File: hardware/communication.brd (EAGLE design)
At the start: 33.5 x 34.6 mm, 34 parts, among them J1 MICRO_USB_B_HIROSE_ZX62-B-5PA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, SW1 TVAF06-A020B-R, U2 NJM12888F, X1 FA-238

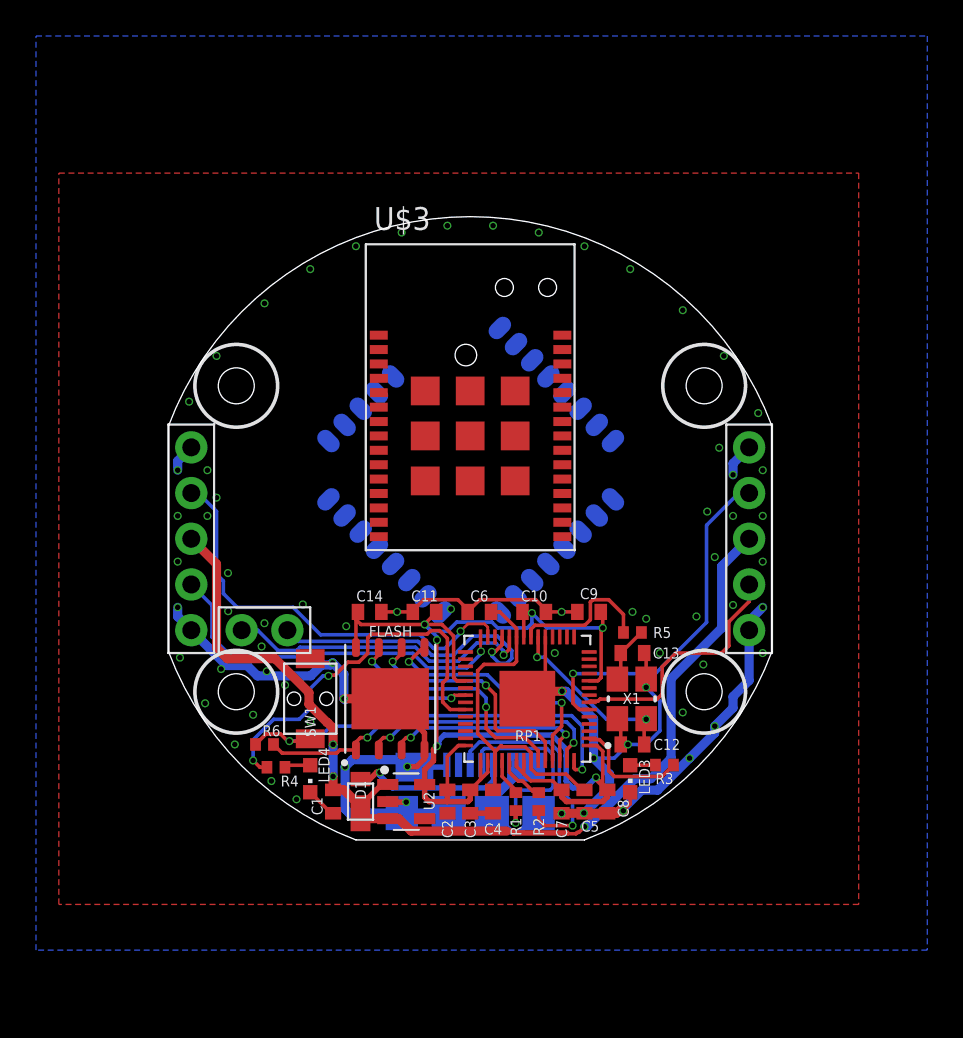
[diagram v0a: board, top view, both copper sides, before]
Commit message: communicationの回路図と基盤の途中経過です。Lo-Raの部分が終わって、残りはTweLiteをやれば完成のはずです。初めて基盤の設計をしているので不備が必ずあると思います。確認お願いします。
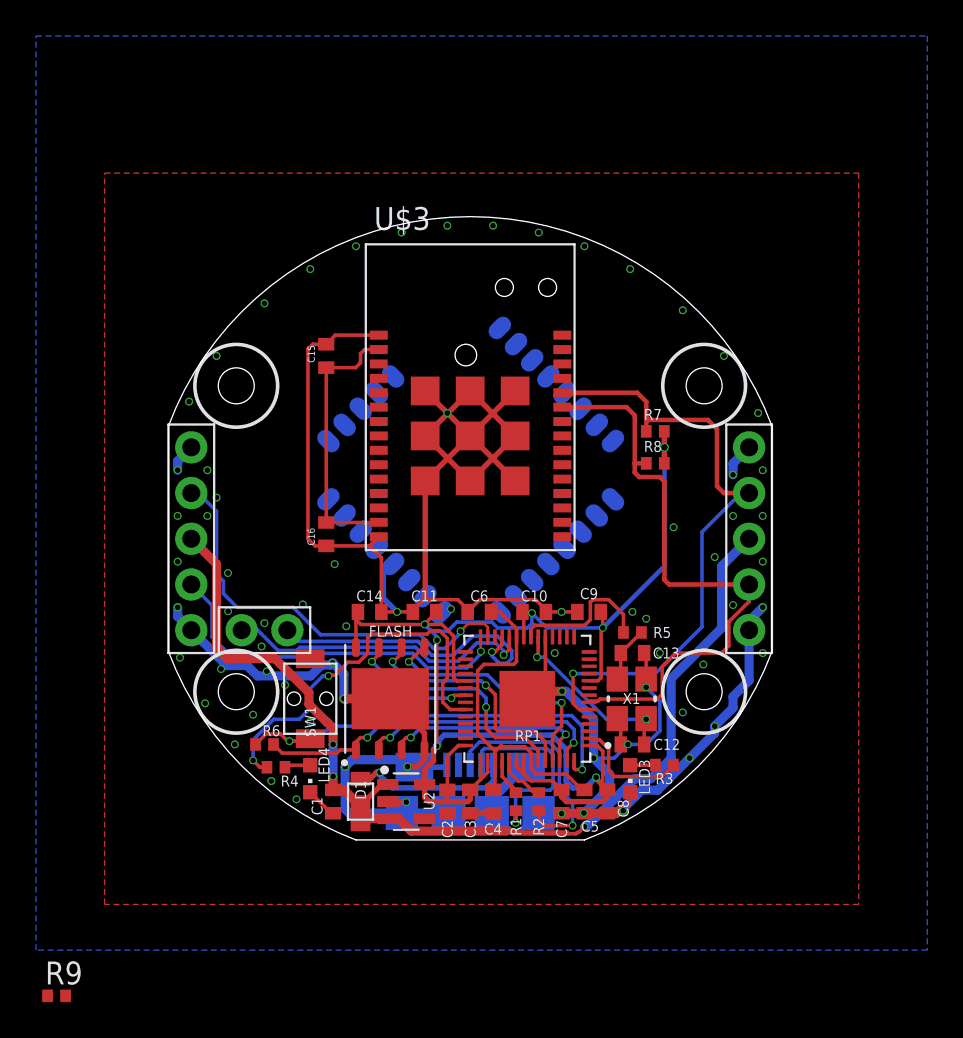
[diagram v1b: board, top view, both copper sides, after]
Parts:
- added C15, C16: 0.1µ, rcl:C0402
- added R7, R8, R9: 10k, rcl:R0402
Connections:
- new net WKUP: R9.1, U$3.P17
- net GND: now also C15.2, C16.1, U$3.P1, U$3.P15, U$3.P31, U$3.P32, U$3.P33, U$3.P34, U$3.P35, U$3.P36, U$3.P37, U$3.P38, U$3.P39
- net RX1: now also R8.1, U$3.P25
- net TX1: now also R7.1, U$3.P26
- net VDD: now also C15.1, C16.2, R7.2, R8.2, R9.2, U$3.P14, U$3.P2
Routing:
- net GND: track 112.9 -> 174.2 mm
- net VDD: track 73.4 -> 101.9 mm, vias 6 -> 7
- net RX1: track 13.8 -> 34.2 mm
- net TX1: track 19.8 -> 35.6 mm

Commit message: communication 回路図、基盤　更新
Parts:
- added C17: 0.1µ, rcl:C0402
- added R10, R11: 10k, rcl:R0402
- added R12, R13: 1k, rcl:R0402
- moved R9 43.6 mm to (11.9, 0.76)
- moved R7 3.58 mm to (11.9, 2.79)
- moved R8 2.92 mm to (11.9, 1.78)
- moved C10 2.42 mm to (3.68, -1.65)
- moved C9 2.42 mm to (6.73, -1.65)
- moved C11 2.41 mm to (-2.54, -1.65)
- moved C14 2.41 mm to (-5.59, -1.65)
- moved C6 2.41 mm to (0.51, -1.65)
- moved C16 0.92 mm to (-7.11, 0.51)
- moved C15 0.89 mm to (-7.11, 10.2)
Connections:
- removed net I2C_SCL: RP1.12
- removed net PWM5_A: RP1.13
- removed net PWM5_B: RP1.14
- removed net SPI0_MISO: RP1.31
- removed net SPI0_MOSI: RP1.30
- removed net SPI0_SCK: RP1.29
- removed net SPI1_CS: RP1.16
- removed net SPI1_MISO: RP1.15
- removed net SPI1_MOSI: RP1.18
- removed net SPI1_SCK: RP1.17
- removed net VCC: U$1.5
- new net ROLA_SCL: R7.1, RP1.16, U$3.P19
- new net ROLA_SDA: R8.1, RP1.15, U$3.P18
- new net TWE_BPS: RP1.31, U$1.19
- new net TWE_PGM: RP1.12, U$1.2
- new net TWE_RESET: R11.2, R12.1, R12.2, RP1.30, U$1.21
- new net TWE_RTS: RP1.13, U$1.7
- new net TWE_RTX: RP1.17, U$1.8
- new net TWE_SLEEP: R10.1, R13.1, R13.2, RP1.29, U$1.27
- new net TWE_TRX: RP1.18, U$1.9
- net GND: now also C17.2, R11.1
- net RX1: no longer R8.1, U$3.P25
- net TX1: no longer R7.1, U$3.P26
- net VDD: now also C17.1, R10.2, U$1.5
- net WKUP: now also RP1.14
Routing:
- net VDD: track 101.9 -> 131.7 mm, vias 7 -> 8
- net TWE_PGM: track 0.00 -> 28.5 mm, vias 0 -> 1
- net TWE_SLEEP: track 0.00 -> 25.1 mm, vias 0 -> 3
- net TWE_RESET: track 0.00 -> 22.7 mm, vias 0 -> 3
- net RX1: track 34.2 -> 13.8 mm
- net TWE_RTS: track 0.00 -> 19.2 mm, vias 0 -> 1
- net ROLA_SCL: track 0.00 -> 17.7 mm, vias 0 -> 2
- net ROLA_SDA: track 0.00 -> 16.5 mm, vias 0 -> 2
- net WKUP: track 0.00 -> 15.9 mm, vias 0 -> 2
- net TX1: track 35.6 -> 19.7 mm
- net TWE_RTX: track 0.00 -> 14.2 mm, vias 0 -> 1
- net TWE_TRX: track 0.00 -> 9.04 mm, vias 0 -> 1
- net TWE_BPS: track 0.00 -> 8.18 mm, vias 0 -> 1
- net 1V2: track 19.7 -> 23.4 mm
- net XOUT1: track 8.16 -> 10.5 mm
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
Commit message: communication基盤一部改良、GNSS基盤
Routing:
- net GND: track 174.2 -> 177.4 mm
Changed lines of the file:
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@@
 <wire x1="4.333" y1="-1.651" x2="4.445" y2="-1.651" width="0.2" layer="1"/>
 <wire x1="-6.731" y1="-15.24" x2="-6.9525" y2="-15.0185" width="0.508" layer="16"/>
-<wire x1="-6.9525" y1="-15.0185" x2="-6.9525" y2="-12.6685" width="0.508" layer="16"/>
+<wire x1="-6.9525" y1="-15.0185" x2="-6.9525" y2="-14.732" width="0.508" layer="16"/>
+<wire x1="-6.9525" y1="-14.732" x2="-6.9525" y2="-12.6685" width="0.508" layer="16"/>
 <wire x1="-6.9525" y1="-12.6685" x2="-6.56" y2="-12.276" width="0.508" layer="16"/>
 <wire x1="-3.8" y1="-15.24" x2="-6.731" y2="-15.24" width="0.508" layer="16"/>
@@
 <via x="-13.081" y="-11.43" extent="1-16" drill="0.3"/>
 <via x="-12.065" y="-9.779" extent="1-16" drill="0.3"/>
-<via x="-9.652" y="-14.478" extent="1-16" drill="0.3"/>
+<via x="-8.509" y="-14.859" extent="1-16" drill="0.3"/>
 <via x="12.954" y="-6.985" extent="1-16" drill="0.3"/>
 <via x="16.256" y="-3.81" extent="1-16" drill="0.3"/>
@@
 <via x="10.541" y="-6.35" extent="1-16" drill="0.3"/>
 <via x="11.811" y="-9.652" extent="1-16" drill="0.3"/>
-<via x="-11.049" y="-13.462" extent="1-16" drill="0.3"/>
+<via x="0.635" y="-15.24" extent="1-16" drill="0.3"/>
 <via x="-8.886" y="-10.1735" extent="1-16" drill="0.3"/>
 <via x="-10.287" y="-8.128" extent="1-16" drill="0.3"/>
@@
 <wire x1="-8.89" y1="-6.665" x2="-8.659484375" y2="-6.895515625" width="0.2" layer="1"/>
 <wire x1="-8.659484375" y1="-6.895515625" x2="-7.6455" y2="-6.8955" width="0.2" layer="1"/>
-<wire x1="-8.89" y1="-14.085" x2="-7.72" y2="-15.255" width="0.2" layer="1"/>
+<wire x1="-8.89" y1="-14.085" x2="-8.376" y2="-14.599" width="0.2" layer="1"/>
+<wire x1="-8.376" y1="-14.599" x2="-7.72" y2="-15.255" width="0.2" layer="1"/>
 <wire x1="-7.72" y1="-15.255" x2="-7.62" y2="-15.255" width="0.2" layer="1"/>
 <wire x1="8.89" y1="-14.085" x2="8.89" y2="-14.732" width="0.2" layer="1"/>
@@
 <wire x1="8.524" y1="8.763" x2="9.017" y2="8.763" width="0.254" layer="1"/>
 <wire x1="9.017" y1="8.763" x2="12.7" y2="5.08" width="0.254" layer="1"/>
+<wire x1="-8.509" y1="-14.859" x2="-7.0795" y2="-14.859" width="0.2" layer="16"/>
+<wire x1="-7.0795" y1="-14.859" x2="-6.9525" y2="-14.732" width="0.2" layer="16"/>
+<wire x1="-8.509" y1="-14.859" x2="-8.376" y2="-14.726" width="0.2" layer="1"/>
+<wire x1="-8.376" y1="-14.726" x2="-8.376" y2="-14.599" width="0.2" layer="1"/>
+<wire x1="-1.27" y1="-15.255" x2="0" y2="-15.255" width="0.3048" layer="1"/>
 <wire x1="11.811" y1="12.7" x2="14.097" y2="10.16" width="0" layer="19" extent="1-1"/>
 <wire x1="16.002" y1="6.985" x2="14.097" y2="10.16" width="0" layer="19" extent="1-1"/>
@@
 <wire x1="6.3165" y1="-15.241" x2="6.35" y2="-15.255" width="0" layer="19" extent="1-1"/>
 <wire x1="-1.27" y1="-15.255" x2="-1.2" y2="-15.24" width="0" layer="19" extent="1-16"/>
-<wire x1="1.27" y1="-15.255" x2="1.2" y2="-15.24" width="0" layer="19" extent="1-16"/>
 <wire x1="-3.49" y1="-12.6605" x2="-3.1" y2="-12.69" width="0" layer="19" extent="16-16"/>
 <wire x1="10.541" y1="-6.35" x2="9.667" y2="-6.35" width="0" layer="19" extent="1-1"/>
@@
 <wire x1="-8.31" y1="-4.287" x2="-7.6525" y2="-4.7915" width="0" layer="19" extent="1-1"/>
 <wire x1="-8.673" y1="-3.442" x2="-8.31" y2="-4.287" width="0" layer="19" extent="1-1"/>
+<wire x1="0.635" y1="-15.24" x2="-8.89" y2="-14.085" width="0" layer="19" extent="1-1"/>
 <wire x1="-8.886" y1="-10.1735" x2="-7.0195" y2="-8.89" width="0" layer="19" extent="1-1"/>
 <wire x1="-13.843" y1="-7.239" x2="-16.129" y2="-6.604" width="0" layer="19" extent="1-1"/>
 <wire x1="-14.732" y1="-9.144" x2="-13.843" y2="-7.239" width="0" layer="19" extent="1-1"/>
-<wire x1="-8.89" y1="-14.085" x2="-6.9525" y2="-12.6685" width="0" layer="19" extent="1-1"/>
-<wire x1="-9.652" y1="-14.478" x2="-8.89" y2="-14.085" width="0" layer="19" extent="1-1"/>
-<wire x1="-11.049" y1="-13.462" x2="-9.652" y2="-14.478" width="0" layer="19" extent="1-1"/>
 <wire x1="-12.065" y1="-9.779" x2="-10.287" y2="-8.128" width="0" layer="19" extent="1-1"/>
 <wire x1="-13.081" y1="-11.43" x2="-12.065" y2="-9.779" width="0" layer="19" extent="1-1"/>
